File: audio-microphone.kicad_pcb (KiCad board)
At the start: 2 copper layers, 20 x 20 mm, 9 parts, among them J1 JST_SH_1x4_BM04B-SRSS-TB-LF-SN

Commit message: [#71550] Start placement
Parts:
- removed C4: C_100p_0402, antmicro-footprints:C_0402_1005Metric
- removed C5: C_100n_16V_X7R_0402, antmicro-footprints:C_0402_1005Metric
- added FB1: FB_600Z_0.5A_Murata-BLM18AG_0603, antmicro-footprints:FB_0603_1608Metric, F.Cu at (239.2, 143.4)
- added R3: R_0R_0402, antmicro-footprints:R_0402_1005Metric, F.Cu at (236.0, 147.8)
- C1: value C_100n_16V_X7R_0402 -> C_220p_0402
- C2: value C_100p_0402 -> C_100n_0402; moved to F.Cu
- C3: value C_100p_0402 -> C_1u_0402; moved to F.Cu
- J1: value JST_SH_1x4_BM04B-SRSS-TB-LF-SN -> JST_SH_1x5_BM05B-SURS-TB-LF-SN; footprint antmicro-footprints:Conn_JST_SH_1x4_BM04B-SRSS-TB-LF-SN -> antmicro-footprints:Conn_JST_SH_1x5_BM05B-SURS-TF-LF-SN
- MK1: value MK_IM73A135V01XTSA1 -> MK_SPH0645LM4H-B; footprint antmicro-footprints:MK_IM73A135V01XTSA1 -> antmicro-footprints:MK_SPH0645LM4H-B
- R1: value R_25k_0402 -> R_51R_0402; moved to F.Cu
- R2: value R_25k_0402 -> R_0R_0402; moved to F.Cu
- moved R1 41.4 mm to (242.0, 147.9), turned to -90 degrees
- moved C2 40.2 mm to (241.8, 143.0), turned to 90 degrees
- moved MK1 40.2 mm to (240.0, 146.9)
- moved J1 40.0 mm to (240.0, 150.2)
- moved C1 38.6 mm to (240.9, 143.3)
- moved R2 37.8 mm to (237.4, 147.3), turned to 0 degrees
- moved C3 37.5 mm to (237.5, 148.3)
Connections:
- C1 pad 2: +2V75 -> VDD
- C2 pad 1: Net-(MK1-OUTPUT+) -> VDD
- C3 pad 1: Net-(MK1-OUTPUT-) -> GND
- C3 pad 2: Net-(MK1-OUTPUT+) -> VCC
- J1 pad 1: GND -> VCC
- J1 pad 2: Net-(J1-Pad2) -> GND
- J1 pad 3: Net-(J1-Pad3) -> /WS
- J1 pad 4: +2V75 -> /BCLK
- MK1 pad 1: Net-(MK1-OUTPUT+) -> /WS
- MK1 pad 2: +2V75 -> /SELECT
- MK1 pad 3: Net-(MK1-OUTPUT-) -> GND
- MK1 pad 4: GND -> /BCLK
- MK1 pad 5: GND -> VDD
- R1 pad 1: Net-(J1-Pad3) -> Net-(MK1-DATA)
- R1 pad 2: Net-(MK1-OUTPUT+) -> /DATA
- R2 pad 1: Net-(MK1-OUTPUT-) -> /SELECT
- R2 pad 2: Net-(J1-Pad2) -> VDD
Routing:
- net +2V75: track 11.9 -> 0.00 mm, vias 1 -> 0
- net /WS: track 0.00 -> 9.31 mm, vias 0 -> 2
- net Net-(MK1-OUTPUT-): track 7.25 -> 0.00 mm, vias 1 -> 0
- net Net-(MK1-OUTPUT+): track 7.24 -> 0.00 mm, vias 1 -> 0
- net /BCLK: track 0.00 -> 5.71 mm
- net Net-(MK1-DATA): track 0.00 -> 3.88 mm, vias 0 -> 2
- net VDD: track 0.00 -> 3.34 mm
- net VCC: track 0.00 -> 3.01 mm
- net /DATA: track 0.00 -> 2.98 mm
- net GND: track 0.48 -> 1.79 mm, vias 26 -> 1
- net Net-(J1-Pad3): track 1.22 -> 0.00 mm, vias 1 -> 0
- net Net-(J1-Pad2): track 1.22 -> 0.00 mm, vias 1 -> 0
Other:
- board size 20 x 20 mm -> 11.5 x 11.5 mm
- board text removed: "Rev.${REVISION} Microphone"
- board text removed: "SHA ########"

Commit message: [#71550] Route connections
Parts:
- J1: value JST_SH_1x5_BM05B-SURS-TB-LF-SN -> JST_SUR_1x5_BM05B-SURS-TB-LF-SN; footprint antmicro-footprints:Conn_JST_SH_1x5_BM05B-SURS-TF-LF-SN -> antmicro-footprints:Conn_JST_SUR_1x5_BM05B-SURS-TF-LF-SN
- moved R3 5.94 mm to (238.2, 142.3), turned to 0 degrees
- moved R2 5.32 mm to (239.2, 142.3)
- moved C2 0.36 mm to (241.5, 143.2)
- moved C1 0.31 mm to (240.6, 143.2)
- moved FB1 0.30 mm to (238.9, 143.4)
- moved R1 0.19 mm to (242.0, 147.7)
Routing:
- net /SELECT: track 0.00 -> 5.84 mm, vias 0 -> 2
- net VCC: track 3.01 -> 8.62 mm
- net GND: track 1.79 -> 7.25 mm, vias 1 -> 8
- net VDD: track 3.34 -> 4.47 mm
- net Net-(MK1-DATA): track 3.88 -> 4.85 mm
- net /WS: track 9.31 -> 8.67 mm
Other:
- outline, holes or cut-outs redrawn
- board text added: "Audio Microphone"
- board text added: "SHA:########"

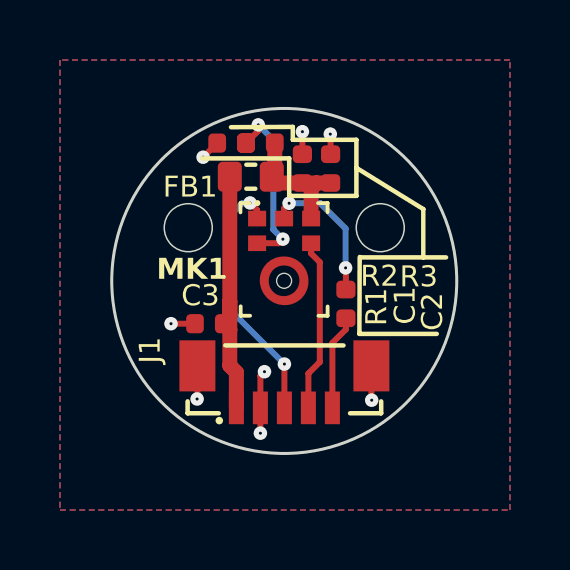
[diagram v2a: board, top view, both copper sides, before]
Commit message: [#71550] Add new mounting system
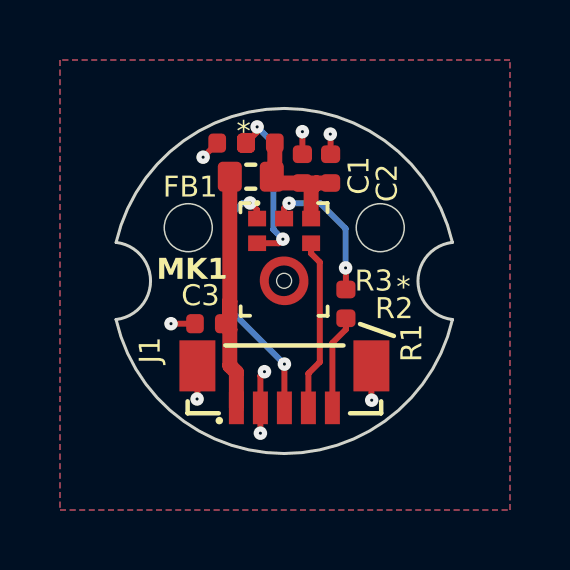
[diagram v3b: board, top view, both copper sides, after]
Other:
- board size 11.5 x 11.5 mm -> 11.2 x 11.5 mm
- board text added: "*"
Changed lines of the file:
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@@
 		(tags "capacitor SMD 0402")
 		(property "Reference" "C2"
-			(at -5.41 3.8 90)
+			(at -1.12 2.29 90)
 			(layer "F.SilkS")
 			(effects
@@
 		(tags "capacitor SMD 0402")
 		(property "Reference" "C1"
-			(at 3.92 -3.01 90)
+			(at -0.41 -1.47 90)
 			(layer "F.SilkS")
 			(effects
@@
 		(tags "resistor SMD 0402")
 		(property "Reference" "R3"
-			(at 5.6 4.86 0)
+			(at 4.1 5 180)
 			(layer "F.SilkS")
 			(effects
@@
 		(tags "resistor SMD 0402")
 		(property "Reference" "R1"
-			(at -0.54 -0.61 -90)
+			(at 0.66 -1.78 -90)
 			(layer "F.SilkS")
 			(effects
@@
 		(tags "resistor SMD 0402")
 		(property "Reference" "R2"
-			(at 3.33 4.84 0)
+			(at 3.82 5.92 180)
 			(layer "F.SilkS")
 			(effects
@@
 	)
 	(gr_line
-		(start 240.14 142.84)
-		(end 240.14 144.09)
+		(start 243.63 148.76)
+		(end 242.5 148.36)
 		(stroke
 			(width 0.15)
@@
 	)
 	(gr_line
-		(start 244.61 144.53)
-		(end 242.38 143.155)
-		(stroke
-			(width 0.15)
-			(type default)
-		)
-		(layer "F.SilkS")
-	)
-	(gr_line
-		(start 242.38 142.22)
-		(end 240.26 142.22)
-		(stroke
-			(width 0.15)
-			(type default)
-		)
-		(layer "F.SilkS")
-	)
-	(gr_line
-		(start 242.53 146.14)
-		(end 245.37 146.14)
-		(stroke
-			(width 0.15)
-			(type default)
-		)
-		(layer "F.SilkS")
-	)
-	(gr_line
-		(start 240.14 144.09)
-		(end 242.38 144.09)
+		(start 239.975 134.8)
+		(end 239.975 160.45)
 		(stroke
 			(width 0.15)
-			(type default)
+			(type dash)
 		)
-		(layer "F.SilkS")
+		(layer "Dwgs.User")
 	)
 	(gr_line
-		(start 242.38 144.09)
-		(end 242.38 142.22)
+		(start 233.260191 143.034847)
+		(end 247.099808 151.025153)
 		(stroke
-			(width 0.15)
-			(type default)
+			(width 0.1)
+			(type dash)
 		)
-		(layer "F.SilkS")
+		(layer "Dwgs.User")
 	)
 	(gr_line
-		(start 237.24 142.84)
-		(end 240.14 142.84)
+		(start 227.875001 146.925)
+		(end 253.524999 146.925)
 		(stroke
 			(width 0.15)
-			(type default)
+			(type dash)
 		)
-		(layer "F.SilkS")
+		(layer "Dwgs.User")
 	)
-	(gr_line
-		(start 244.61 146.14)
-		(end 244.61 144.53)
+	(gr_arc
+		(start 244.42 150.59)
+		(mid 244.088896 149.261761)
+		(end 245.394692 148.850977)
 		(stroke
 			(width 0.15)
 			(type default)
 		)
-		(layer "F.SilkS")
+		(layer "Dwgs.User")
 	)
-	(gr_line
-		(start 242.49 146.125)
-		(end 242.48 148.69)
+	(gr_arc
+		(start 235.58 143.19)
+		(mid 235.867471 144.516255)
+		(end 234.571351 144.918328)
 		(stroke
 			(width 0.15)
 			(type default)
 		)
-		(layer "F.SilkS")
+		(layer "Dwgs.User")
 	)
-	(gr_line
-		(start 240.26 142.22)
-		(end 240.26 141.79)
+	(gr_arc
+		(start 245.579999 148.21)
+		(mid 244.431845 146.923896)
+		(end 245.582194 145.639754)
 		(stroke
-			(width 0.15)
+			(width 0.1)
 			(type default)
 		)
-		(layer "F.SilkS")
+		(layer "Edge.Cuts")
 	)
-	(gr_line
-		(start 242.48 148.69)
-		(end 245.06 148.69)
+	(gr_circle
+		(center 243.175 145.15)
+		(end 243.975 145.15)
 		(stroke
-			(width 0.15)
+			(width 0.05)
 			(type default)
 		)
-		(layer "F.SilkS")
+		(fill none)
+		(layer "Edge.Cuts")
 	)
-	(gr_line
-		(start 240.26 141.79)
-		(end 238.2 141.8)
+	(gr_arc
+		(start 234.37 145.64)
+		(mid 239.975125 141.174587)
+		(end 245.580056 145.640244)
 		(stroke
-			(width 0.15)
+			(width 0.1)
 			(type default)
 		)
-		(layer "F.SilkS")
-	)
-	(gr_line
-		(start 239.975 134.8)
-		(end 239.975 160.45)
-		(stroke
-			(width 0.15)
-			(type dash)
-		)
-		(layer "Dwgs.User")
-	)
-	(gr_line
-		(start 227.875001 146.925)
-		(end 253.524999 146.925)
-		(stroke
-			(width 0.15)
-			(type dash)
-		)
-		(layer "Dwgs.User")
+		(layer "Edge.Cuts")
 	)
-	(gr_circle
-		(center 239.975 146.925)
-		(end 245.725 146.925)
+	(gr_arc
+		(start 234.37 145.64)
+		(mid 235.518154 146.926104)
+		(end 234.367805 148.210246)
 		(stroke
 			(width 0.1)
 			(type default)
 		)
-		(fill none)
 		(layer "Edge.Cuts")
 	)
 	(gr_circle
-		(center 243.175 145.15)
-		(end 243.975 145.15)
+		(center 236.775 145.15)
+		(end 237.575 145.15)
 		(stroke
 			(width 0.05)
@@
 		(layer "Edge.Cuts")
 	)
-	(gr_circle
-		(center 236.775 145.15)
-		(end 237.575 145.15)
+	(gr_arc
+		(start 245.582138 148.21049)
+		(mid 239.974875 152.677606)
+		(end 234.367805 148.210246)
 		(stroke
-			(width 0.05)
+			(width 0.1)
 			(type default)
 		)
-		(fill none)
 		(layer "Edge.Cuts")
 	)
@@
 		)
 	)
+	(gr_text "*"
+		(at 238.38 142.35 0)
+		(layer "F.SilkS")
+		(effects
+			(font
+				(size 0.7 0.7)
+				(thickness 0.15)
+			)
+			(justify left bottom)
+		)
+	)
+	(gr_text "*"
+		(at 243.71 147.54 0)
+		(layer "F.SilkS")
+		(effects
+			(font
+				(size 0.7 0.7)
+				(thickness 0.15)
+			)
+			(justify left bottom)
+		)
+	)
 	(dimension
 		(type aligned)
@@
 	)
 	(segment
-		(start 239.110006 141.919994)
+		(start 239.070932 141.959068)
 		(end 238.7 142.33)
 		(width 0.2)
@@
 	)
 	(segment
-		(start 239.110006 141.722455)
-		(end 239.110006 141.919994)
+		(start 239.070932 141.789913)
+		(end 239.070932 141.959068)
 		(width 0.2)
 		(layer "F.Cu")
@@
 	)
 	(via
-		(at 239.110006 141.722455)
+		(at 239.070932 141.789913)
 		(size 0.45)
 		(drill 0.1)
@@
 	(segment
 		(start 239.611511 145.213513)
-		(end 239.611511 142.22396)
+		(end 239.93 145.532002)
 		(width 0.2)
 		(layer "B.Cu")
@@
 	)
 	(segment
-		(start 239.93 145.532002)
-		(end 239.611511 145.213513)
+		(start 239.070932 141.789913)
+		(end 239.611511 142.330492)
 		(width 0.2)
 		(layer "B.Cu")
@@
 	)
 	(segment
-		(start 239.611511 142.22396)
-		(end 239.110006 141.722455)
+		(start 239.611511 142.330492)
+		(end 239.611511 145.213513)
 		(width 0.2)
 		(layer "B.Cu")

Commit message: [#71550] Swap BCLK and WS, Fix outline
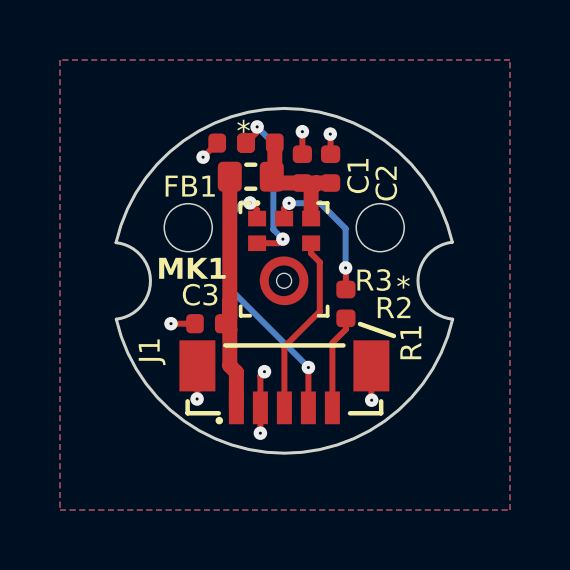
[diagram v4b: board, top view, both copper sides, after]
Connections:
- J1 pad 3: /WS -> /BCLK
- J1 pad 4: /BCLK -> /WS
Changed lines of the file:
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@@
 			(size 0.5 1.0922)
 			(layers "F.Cu" "F.Paste" "F.Mask")
-			(net 4 "/WS")
+			(net 6 "/BCLK")
 			(pintype "passive")
 		)
@@
 			(size 0.5 1.0922)
 			(layers "F.Cu" "F.Paste" "F.Mask")
-			(net 6 "/BCLK")
+			(net 4 "/WS")
 			(pintype "passive")
 		)
@@
 	)
 	(gr_arc
-		(start 245.579999 148.21)
-		(mid 244.431845 146.923896)
-		(end 245.582194 145.639754)
+		(start 245.59 148.199999)
+		(mid 244.432261 146.921531)
+		(end 245.579299 145.633453)
 		(stroke
 			(width 0.1)
@@
 	)
 	(gr_arc
-		(start 234.37 145.64)
-		(mid 239.975125 141.174587)
-		(end 245.580056 145.640244)
+		(start 234.368012 145.648922)
+		(mid 239.966236 141.174642)
+		(end 245.578072 145.631837)
 		(stroke
 			(width 0.1)
@@
 	)
 	(gr_arc
-		(start 234.37 145.64)
-		(mid 235.518154 146.926104)
-		(end 234.367805 148.210246)
+		(start 234.368011 145.648922)
+		(mid 235.515828 146.920905)
+		(end 234.375667 148.199756)
 		(stroke
 			(width 0.1)
@@
 	)
 	(gr_arc
-		(start 245.582138 148.21049)
-		(mid 239.974875 152.677606)
-		(end 234.367805 148.210246)
+		(start 245.59 148.2)
+		(mid 239.982737 152.667116)
+		(end 234.375667 148.199756)
 		(stroke
 			(width 0.1)
@@
 	)
 	(segment
-		(start 239.98 149.696)
-		(end 239.98 151.155)
+		(start 240.78 151.155)
+		(end 240.78 149.81)
 		(width 0.2)
 		(layer "F.Cu")
@@
 	)
 	(via
-		(at 239.98 149.696)
+		(at 240.78 149.81)
 		(size 0.45)
 		(drill 0.1)
@@
 	(segment
 		(start 238.584739 144.325261)
+		(end 238.835 144.325261)
+		(width 0.2)
+		(layer "B.Cu")
+		(net 4)
+	)
+	(segment
+		(start 238.11 147.132572)
 		(end 238.11 144.8)
 		(width 0.2)
@@
 	)
 	(segment
-		(start 238.11 144.8)
-		(end 238.11 147.826)
+		(start 240.78 149.802572)
+		(end 238.11 147.132572)
 		(width 0.2)
 		(layer "B.Cu")
@@
 	)
 	(segment
-		(start 238.835 144.325261)
+		(start 238.11 144.8)
 		(end 238.584739 144.325261)
 		(width 0.2)
@@
 	)
 	(segment
-		(start 238.11 147.826)
-		(end 239.98 149.696)
+		(start 240.78 149.81)
+		(end 240.78 149.802572)
 		(width 0.2)
 		(layer "B.Cu")
@@
 	)
 	(segment
-		(start 240.779999 150.010001)
-		(end 240.779999 151.155)
+		(start 239.98 149.12)
+		(end 239.98 151.155)
 		(width 0.2)
 		(layer "F.Cu")
@@
 	)
 	(segment
-		(start 241.16 149.63)
-		(end 240.779999 150.010001)
+		(start 241.16 147.94)
+		(end 239.98 149.12)
 		(width 0.2)
 		(layer "F.Cu")
@@
 	)
 	(segment
-		(start 241.16 146.3)
-		(end 241.16 149.63)
+		(start 240.87 145.668)
+		(end 240.87 146.01)
 		(width 0.2)
 		(layer "F.Cu")
@@
 	)
 	(segment
-		(start 240.87 145.668)
-		(end 240.87 146.01)
+		(start 240.87 146.01)
+		(end 241.16 146.3)
 		(width 0.2)
 		(layer "F.Cu")
@@
 	)
 	(segment
-		(start 240.87 146.01)
-		(end 241.16 146.3)
+		(start 241.16 146.3)
+		(end 241.16 147.94)
 		(width 0.2)
 		(layer "F.Cu")
